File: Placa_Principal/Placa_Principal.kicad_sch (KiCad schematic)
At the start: 2 parts, among them U2 ESP32-S3-DevKitC

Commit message: Segundo commit
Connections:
- net ESP_GPIO17: now reaches U2.10 (GPIO17/ADC2_CH6)
- net ESP_GPIO18: now reaches U2.11 (GPIO18/ADC2_CH7)
- net ESP_GPIO08: now reaches U2.12 (GPIO8/ADC1_CH7)
- net ESP_GPIO03: now reaches U2.13 (GPIO3/ADC1_CH2)
- net ESP_GPIO46: now reaches U2.14 (GPIO46)
- net ESP_GPIO09: now reaches U2.15 (GPIO9/ADC1_CH8)
- net SPI: now reaches U2.16 (GPIO10/ADC1_CH9)
- net SPI: now also U2.17 (GPIO11/ADC2_CH0), U2.18 (GPIO12/ADC2_CH1), U2.19 (GPIO13/ADC2_CH2)
- net ESP_GPIO14: now reaches U2.20 (GPIO14/ADC2_CH3)
- net ESP_GPIO45: now reaches U2.30 (GPIO45)
- net ESP_GPIO04: now reaches U2.4 (GPIO4/ADC1_CH3)
- net ESP_GPIO05: now reaches U2.5 (GPIO5/ADC1_CH4)
- net ESP_GPIO06: now reaches U2.6 (GPIO6/ADC1_CH5)
- net ESP_GPIO07: now reaches U2.7 (GPIO7/ADC1_CH6)
- net ESP_GPIO15: now reaches U2.8 (GPIO15/ADC2_CH4/32K_P)
- net ESP_GPIO16: now reaches U2.9 (GPIO16/ADC2_CH5/32K_N)
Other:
- added sheet Ativacao_Chute (Ativacao_Chute.kicad_sch)
- added sheet Leitura_Encoders (Leitura_Encoders.kicad_sch)

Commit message: Apagar o esquemático de Ativação de Chute
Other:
- removed sheet Ativacao_Chute
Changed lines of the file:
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@@
 	)
 	(sheet
-		(at 24.13 128.27)
-		(size 39.37 13.97)
-		(exclude_from_sim no)
-		(in_bom yes)
-		(on_board yes)
-		(dnp no)
-		(fields_autoplaced yes)
-		(stroke
-			(width 0.1524)
-			(type solid)
-		)
-		(fill
-			(color 0 0 0 0.0000)
-		)
-		(property "Sheetname" "Ativacao_Chute"
-			(at 24.13 127.5584 0)
-			(effects
-				(font
-					(size 1.27 1.27)
-				)
-				(justify left bottom)
-			)
-		)
-		(property "Sheetfile" "Ativacao_Chute.kicad_sch"
-			(at 24.13 142.8246 0)
-			(effects
-				(font
-					(size 1.27 1.27)
-				)
-				(justify left top)
-			)
-		)
-		(instances
-			(project "Placa_Principal"
-				(path "/02649df7-f0d0-431b-8f11-0967d1dd03be"
-					(page "7")
-				)
-			)
-		)
-	)
-	(sheet
-		(at 24.13 151.13)
+		(at 24.13 130.81)
 		(size 39.37 13.97)
 		(exclude_from_sim no)
@@
 		)
 		(property "Sheetname" "Leitura_Encoders"
-			(at 24.13 150.4184 0)
+			(at 24.13 130.0984 0)
 			(effects
 				(font
@@
 		)
 		(property "Sheetfile" "Leitura_Encoders.kicad_sch"
-			(at 24.13 165.6846 0)
+			(at 24.13 145.3646 0)
 			(effects
 				(font

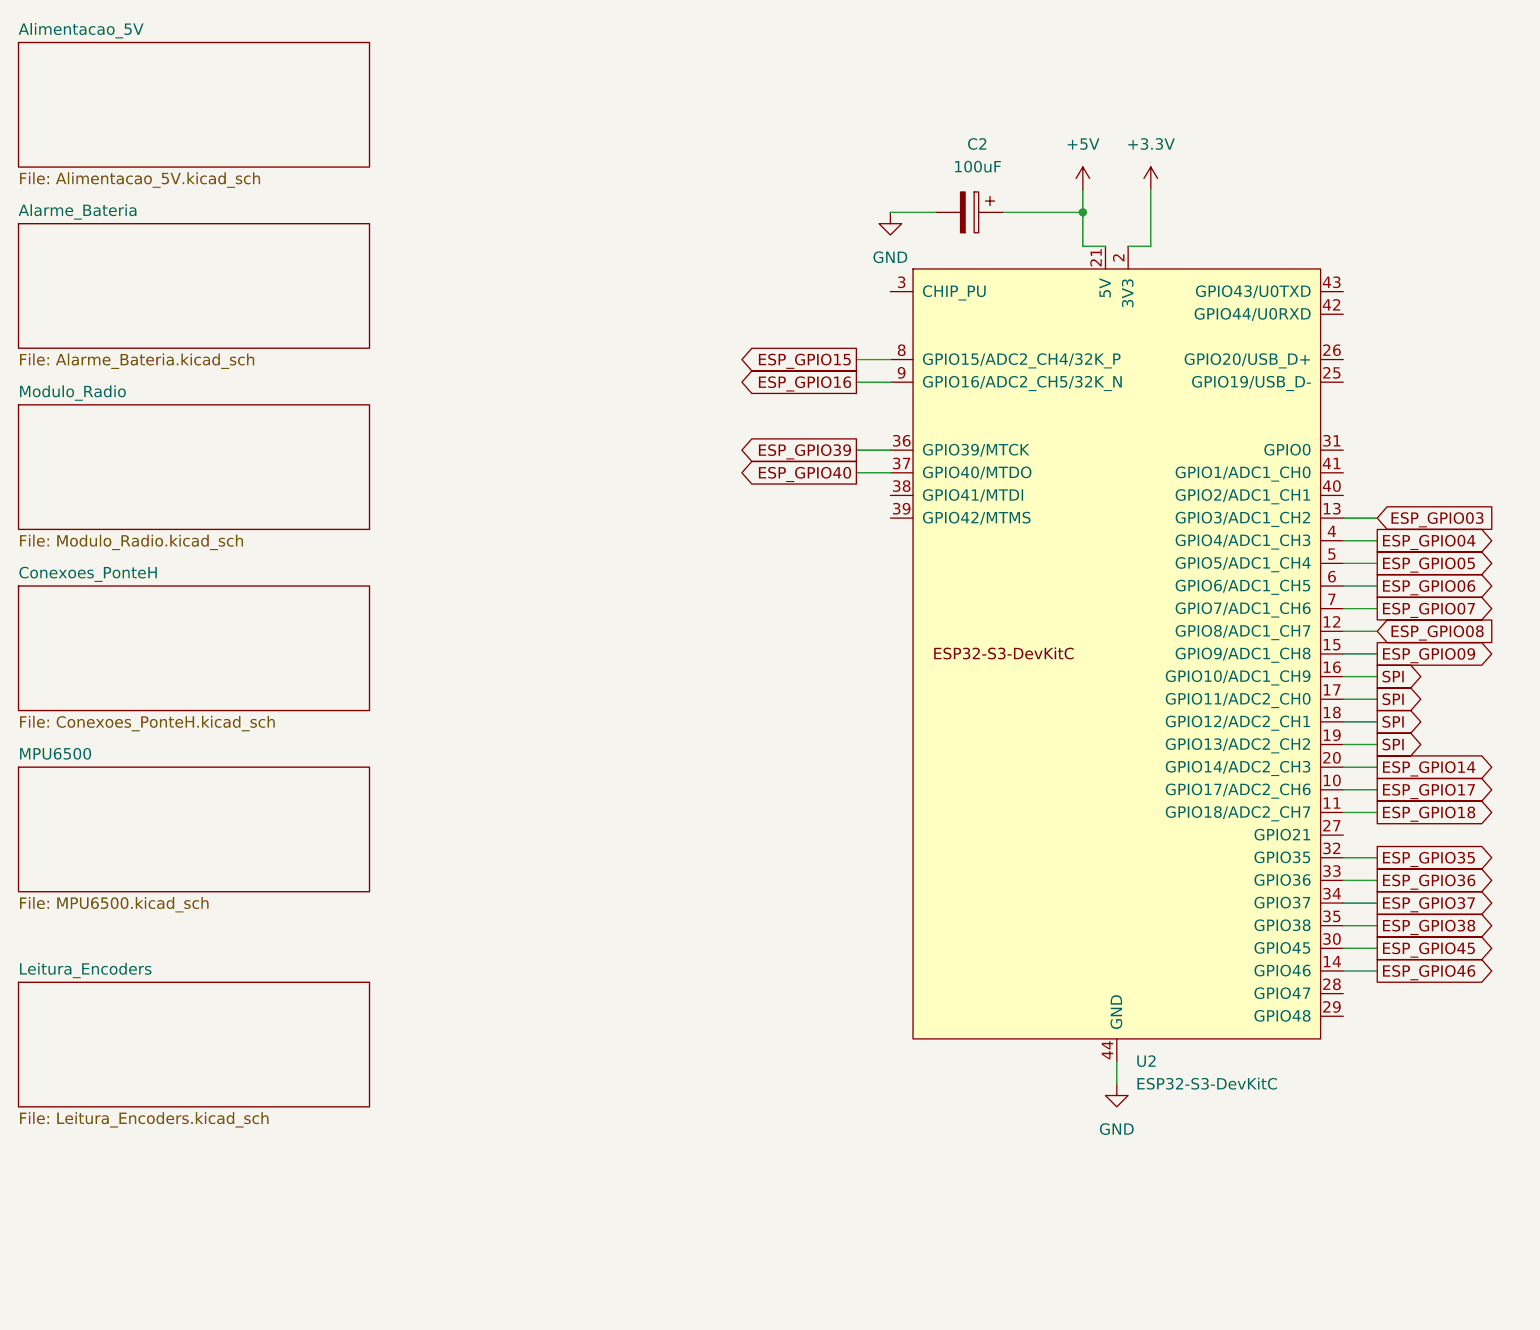
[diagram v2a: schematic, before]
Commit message: Finalizando o esquemático e rearranjando a posição dos componentes na PCB
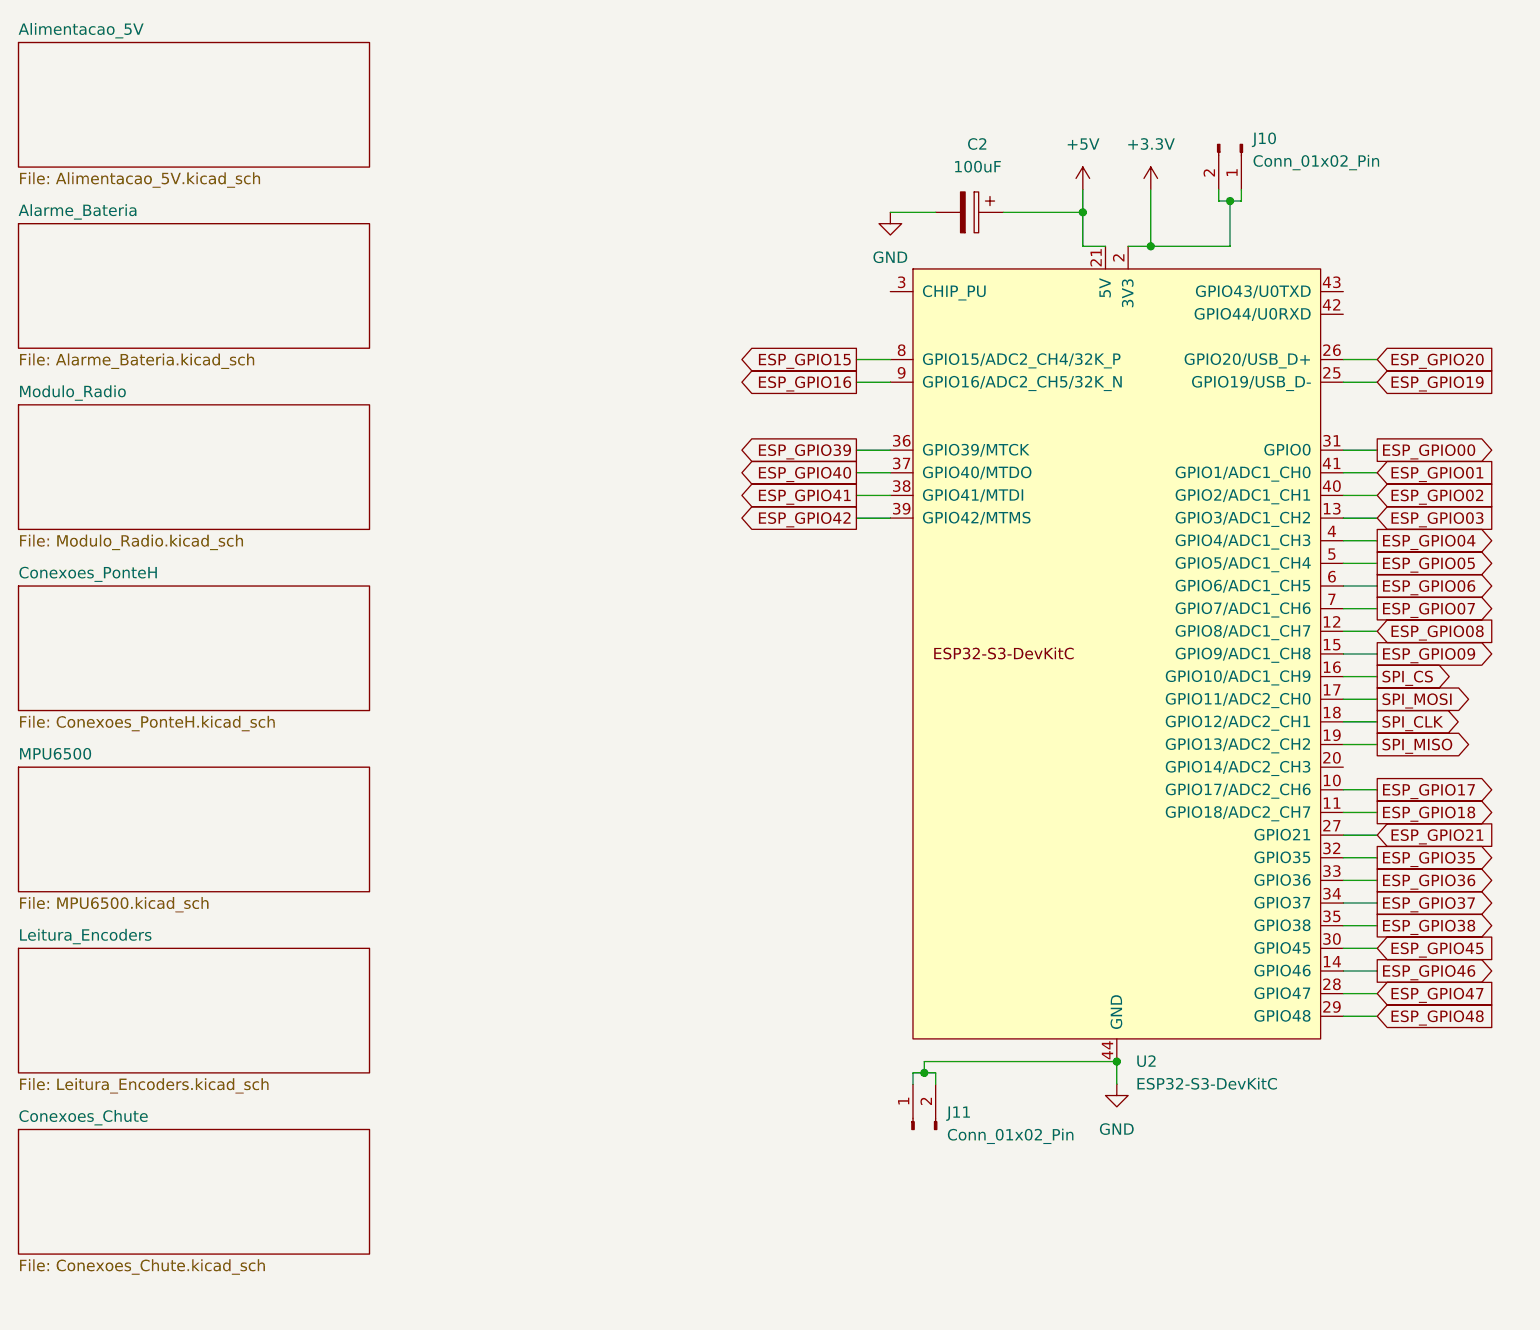
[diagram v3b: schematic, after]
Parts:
- added J10, J11: Conn_01x02_Pin, Connector_PinHeader_2.54mm:PinHeader_1x02_P2.54mm_Vertical, symbol Connector:Conn_01x02_Pin
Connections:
- net +3.3V: now also J10.1 (Pin_1), J10.2 (Pin_2)
- net GND: now also J11.1 (Pin_1), J11.2 (Pin_2)
- net ESP_GPIO19: now reaches U2.25 (GPIO19/USB_D-)
- net ESP_GPIO20: now reaches U2.26 (GPIO20/USB_D+)
- net ESP_GPIO21: now reaches U2.27 (GPIO21)
- net ESP_GPIO47: now reaches U2.28 (GPIO47)
- net ESP_GPIO48: now reaches U2.29 (GPIO48)
- net ESP_GPIO00: now reaches U2.31 (GPIO0)
- net ESP_GPIO41: now reaches U2.38 (GPIO41/MTDI)
- net ESP_GPIO42: now reaches U2.39 (GPIO42/MTMS)
- net ESP_GPIO02: now reaches U2.40 (GPIO2/ADC1_CH1)
- net ESP_GPIO01: now reaches U2.41 (GPIO1/ADC1_CH0)
- net ESP_GPIO14: no longer names the net of U2.20 (GPIO14/ADC2_CH3)
- removed net SPI: U2.16 (GPIO10/ADC1_CH9), U2.17 (GPIO11/ADC2_CH0), U2.18 (GPIO12/ADC2_CH1), U2.19 (GPIO13/ADC2_CH2)
- new net SPI_CLK: U2.18 (GPIO12/ADC2_CH1)
- new net SPI_CS: U2.16 (GPIO10/ADC1_CH9)
- new net SPI_MISO: U2.19 (GPIO13/ADC2_CH2)
- new net SPI_MOSI: U2.17 (GPIO11/ADC2_CH0)
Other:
- added sheet Conexoes_Chute (Conexoes_Chute.kicad_sch)

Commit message: Atualizando a alimentação de todos os sensores e ESP para 3.3V e finalizando o design do monitoramento da bateria e feedback geral
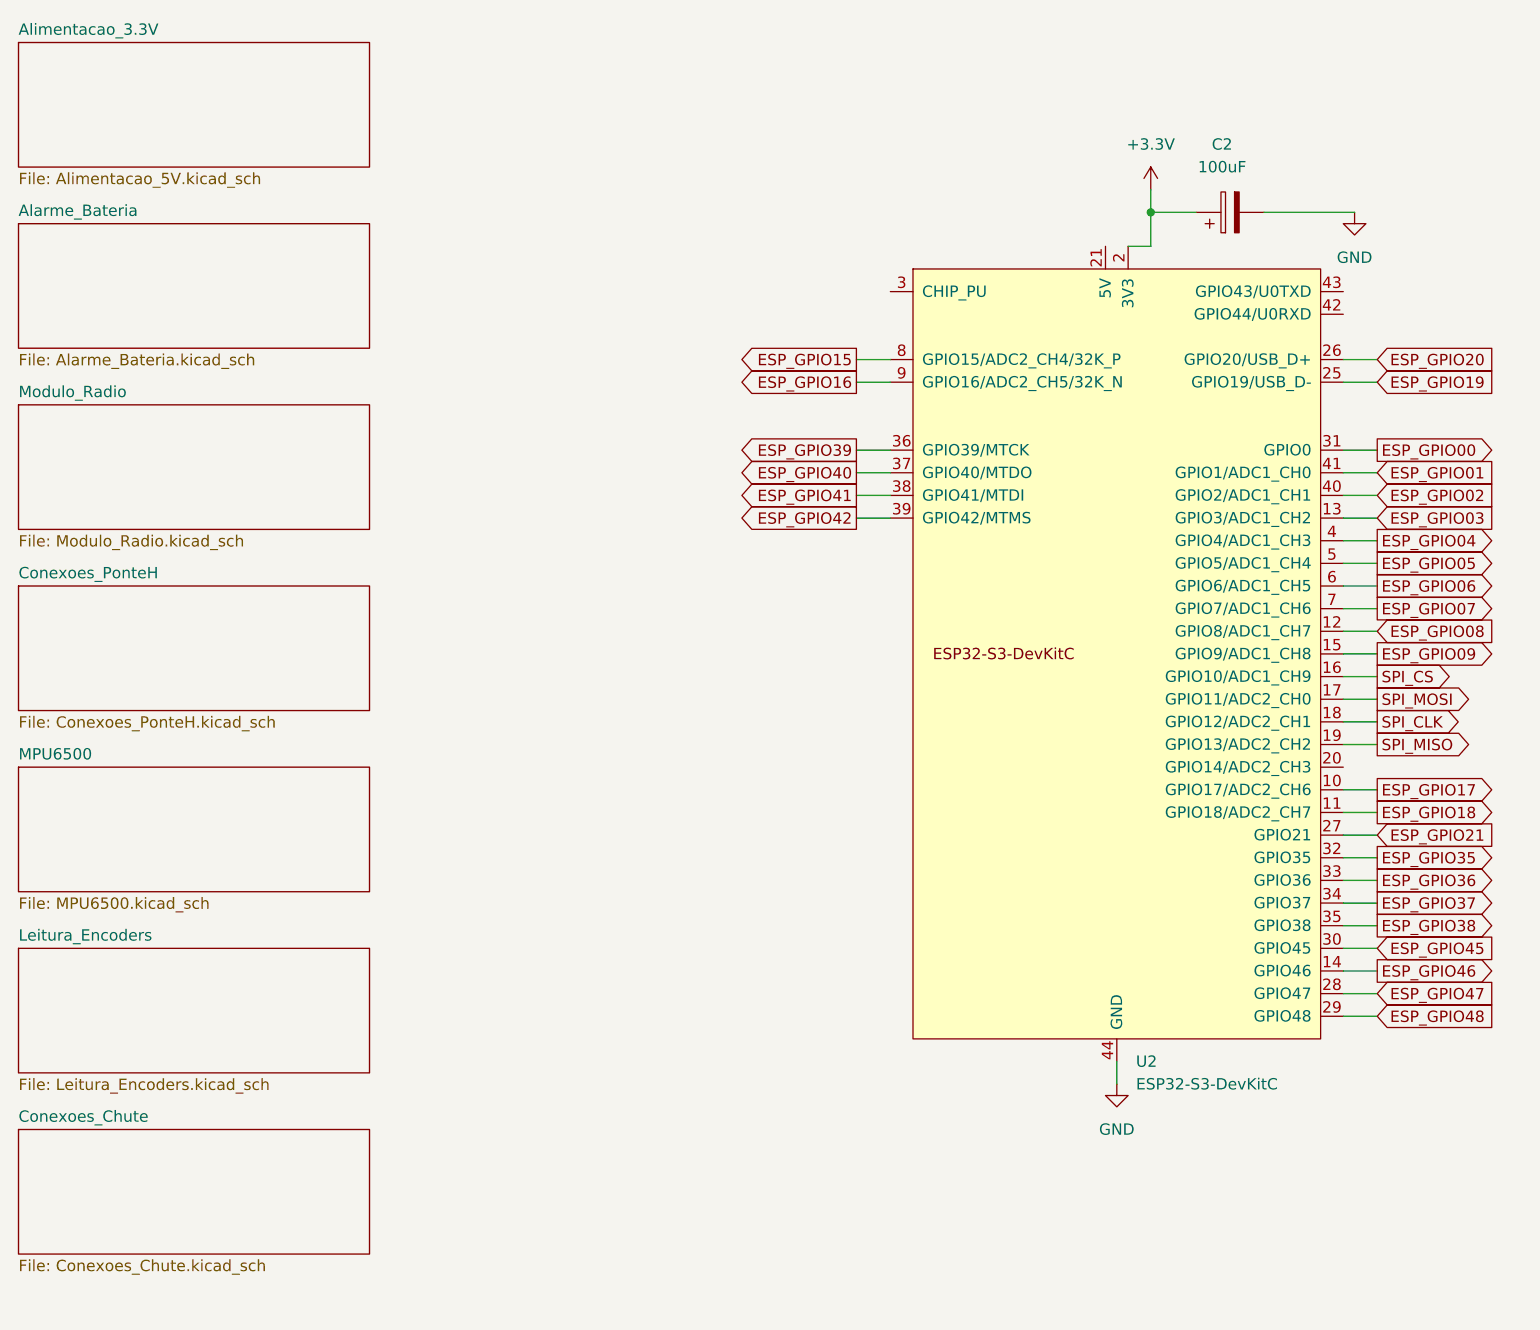
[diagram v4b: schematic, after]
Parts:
- removed J10, J11: Conn_01x02_Pin, Connector_PinHeader_2.54mm:PinHeader_1x02_P2.54mm_Vertical, symbol Connector:Conn_01x02_Pin
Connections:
- net +3.3V: now also C2.1
- net +5V: no longer names the net of U2.21 (5V)
- net +5V: no longer C2.1
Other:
- sheet Alimentacao_5V renamed Alimentacao_3.3V
- moved on the sheet: C2
